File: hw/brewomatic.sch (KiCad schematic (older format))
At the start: 21 parts, among them J1 CON_MAX31865, J2 EXP1, J3 EXP2, J4 12V_IN, J5 12V_ALIM_CONN, J6 HEATING_CONN, J7 PUMP_CONN, Q1 BT139-600, Q2 IRF540N, U1 MOC3021M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

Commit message: Start layout of pcb
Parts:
- added J8: 12V_ALIM_CONN, Connectors_Terminal_Blocks:TerminalBlock_Pheonix_MKDS1.5-2pol, symbol Screw_Terminal_01x02
- J4, J6, J7: footprint Connectors_Terminal_Blocks:TerminalBlock_Pheonix_MPT-2.54mm_2pol -> Connectors_Terminal_Blocks:TerminalBlock_Pheonix_MKDS1.5-2pol
- J5: value 12V_ALIM_CONN -> 230V_CONN; footprint Connectors_Terminal_Blocks:TerminalBlock_Pheonix_MPT-2.54mm_2pol -> Connectors_Terminal_Blocks:TerminalBlock_Pheonix_MKDS1.5-2pol
- Q1: footprint TO_SOT_Packages_THT:TO-220_Neutral123_Vertical -> TO_SOT_Packages_THT:TO-220_Vertical
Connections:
- wire segments 94 -> 96
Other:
- moved on the sheet: J5
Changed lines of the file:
@@
 F 0 "Q1" H 5700 4475 50  0000 L CNN
 F 1 "BT139-600" H 5700 4400 50  0000 L CNN
-F 2 "TO_SOT_Packages_THT:TO-220_Neutral123_Vertical" H 5700 4325 50  0001 L CIN
+F 2 "TO_SOT_Packages_THT:TO-220_Vertical" H 5700 4325 50  0001 L CIN
 F 3 "" H 5500 4400 50  0000 L CNN
 	1    5500 4400
@@
 Wire Wire Line
 	8550 4650 8350 4650
-$Comp
-L +5V #PWR011
-U 1 1 5AB89F21
-P 7550 1650
-F 0 "#PWR011" H 7550 1500 50  0001 C CNN
-F 1 "+5V" H 7550 1790 50  0000 C CNN
-F 2 "" H 7550 1650 50  0001 C CNN
-F 3 "" H 7550 1650 50  0001 C CNN
-	1    7550 1650
-	1    0    0    -1
-$EndComp
 Wire Wire Line
 	7150 1650 7550 1650
@@
 F 0 "J4" H 4300 1200 50  0000 C CNN
 F 1 "12V_IN" H 4300 900 50  0000 C CNN
-F 2 "Connectors_Terminal_Blocks:TerminalBlock_Pheonix_MPT-2.54mm_2pol" H 4300 1100 50  0001 C CNN
+F 2 "Connectors_Terminal_Blocks:TerminalBlock_Pheonix_MKDS1.5-2pol" H 4300 1100 50  0001 C CNN
 F 3 "" H 4300 1100 50  0001 C CNN
 	1    4300 1100
@@
 $EndComp
 $Comp
-L GND #PWR012
+L GND #PWR011
 U 1 1 5AB9867E
 P 3700 1200
-F 0 "#PWR012" H 3700 950 50  0001 C CNN
+F 0 "#PWR011" H 3700 950 50  0001 C CNN
 F 1 "GND" H 3700 1050 50  0000 C CNN
 F 2 "" H 3700 1200 50  0001 C CNN
@@
 	3700 1200 4100 1200
 $Comp
-L +5V #PWR013
+L +5V #PWR012
 U 1 1 5AB987A9
 P 9250 2900
-F 0 "#PWR013" H 9250 2750 50  0001 C CNN
+F 0 "#PWR012" H 9250 2750 50  0001 C CNN
 F 1 "+5V" H 9250 3040 50  0000 C CNN
 F 2 "" H 9250 2900 50  0001 C CNN
@@
 	9250 2950 9250 2900
 $Comp
-L +12V #PWR014
+L +12V #PWR013
 U 1 1 5AB98837
 P 3700 1100
-F 0 "#PWR014" H 3700 950 50  0001 C CNN
+F 0 "#PWR013" H 3700 950 50  0001 C CNN
 F 1 "+12V" H 3700 1240 50  0000 C CNN
 F 2 "" H 3700 1100 50  0001 C CNN
@@
 	8550 3850 8150 3850
 $Comp
-L +3.3V #PWR015
+L +3.3V #PWR014
 U 1 1 5AB9D6E8
 P 9150 2750
-F 0 "#PWR015" H 9150 2600 50  0001 C CNN
+F 0 "#PWR014" H 9150 2600 50  0001 C CNN
 F 1 "+3.3V" H 9150 2890 50  0000 C CNN
 F 2 "" H 9150 2750 50  0001 C CNN
@@
 	9150 2950 9150 2750
 $Comp
-L +12V #PWR016
+L +12V #PWR015
 U 1 1 5AB9D78B
 P 8950 2800
-F 0 "#PWR016" H 8950 2650 50  0001 C CNN
+F 0 "#PWR015" H 8950 2650 50  0001 C CNN
 F 1 "+12V" H 8950 2940 50  0000 C CNN
 F 2 "" H 8950 2800 50  0001 C CNN
@@
 	8950 2950 8950 2800
 $Comp
-L GND #PWR017
+L GND #PWR016
 U 1 1 5AB9DCD3
 P 9050 5150
-F 0 "#PWR017" H 9050 4900 50  0001 C CNN
+F 0 "#PWR016" H 9050 4900 50  0001 C CNN
 F 1 "GND" H 9050 5000 50  0000 C CNN
 F 2 "" H 9050 5150 50  0001 C CNN
@@
 F 0 "J6" H 6550 5000 50  0000 C CNN
 F 1 "HEATING_CONN" H 6550 4700 50  0000 C CNN
-F 2 "Connectors_Terminal_Blocks:TerminalBlock_Pheonix_MPT-2.54mm_2pol" H 6550 4900 50  0001 C CNN
+F 2 "Connectors_Terminal_Blocks:TerminalBlock_Pheonix_MKDS1.5-2pol" H 6550 4900 50  0001 C CNN
 F 3 "" H 6550 4900 50  0001 C CNN
 	1    6550 4900
@@
 $EndComp
 $Comp
-L LINE #PWR018
+L LINE #PWR017
 U 1 1 5ABA2F2E
 P 5500 3850
-F 0 "#PWR018" H 5500 3700 50  0001 C CNN
+F 0 "#PWR017" H 5500 3700 50  0001 C CNN
 F 1 "LINE" H 5500 4000 50  0000 C CNN
 F 2 "" H 5500 3850 50  0001 C CNN
@@
 L Screw_Terminal_01x02 J5
 U 1 1 5ABA346E
-P 3000 1100
-F 0 "J5" H 3000 1200 50  0000 C CNN
-F 1 "12V_ALIM_CONN" H 3000 900 50  0000 C CNN
-F 2 "Connectors_Terminal_Blocks:TerminalBlock_Pheonix_MPT-2.54mm_2pol" H 3000 1100 50  0001 C CNN
-F 3 "" H 3000 1100 50  0001 C CNN
-	1    3000 1100
-	1    0    0    -1
-$EndComp
-$Comp
-L LINE #PWR019
+P 1750 1100
+F 0 "J5" H 1750 1200 50  0000 C CNN
+F 1 "230V_CONN" H 1750 900 50  0000 C CNN
+F 2 "Connectors_Terminal_Blocks:TerminalBlock_Pheonix_MKDS1.5-2pol" H 1750 1100 50  0001 C CNN
+F 3 "" H 1750 1100 50  0001 C CNN
+	1    1750 1100
+	1    0    0    -1
+$EndComp
+$Comp
+L LINE #PWR018
 U 1 1 5ABA3758
-P 2400 1200
-F 0 "#PWR019" H 2400 1050 50  0001 C CNN
-F 1 "LINE" H 2400 1350 50  0000 C CNN
-F 2 "" H 2400 1200 50  0001 C CNN
-F 3 "" H 2400 1200 50  0001 C CNN
-	1    2400 1200
+P 1150 1200
+F 0 "#PWR018" H 1150 1050 50  0001 C CNN
+F 1 "LINE" H 1150 1350 50  0000 C CNN
+F 2 "" H 1150 1200 50  0001 C CNN
+F 3 "" H 1150 1200 50  0001 C CNN
+	1    1150 1200
 	1    0    0    1
 $EndComp
 $Comp
+L NEUT #PWR019
+U 1 1 5ABA379C
+P 1150 1100
+F 0 "#PWR019" H 1150 950 50  0001 C CNN
+F 1 "NEUT" H 1150 1250 50  0000 C CNN
+F 2 "" H 1150 1100 50  0001 C CNN
+F 3 "" H 1150 1100 50  0001 C CNN
+	1    1150 1100
+	1    0    0    -1
+$EndComp
+Wire Wire Line
+	1150 1100 1550 1100
+Wire Wire Line
+	1150 1200 1550 1200
+$Comp
 L NEUT #PWR020
-U 1 1 5ABA379C
-P 2400 1100
-F 0 "#PWR020" H 2400 950 50  0001 C CNN
-F 1 "NEUT" H 2400 1250 50  0000 C CNN
-F 2 "" H 2400 1100 50  0001 C CNN
-F 3 "" H 2400 1100 50  0001 C CNN
-	1    2400 1100
-	1    0    0    -1
-$EndComp
-Wire Wire Line
-	2400 1100 2800 1100
-Wire Wire Line
-	2400 1200 2800 1200
-$Comp
-L NEUT #PWR021
 U 1 1 5ABA6182
 P 6100 4900
-F 0 "#PWR021" H 6100 4750 50  0001 C CNN
+F 0 "#PWR020" H 6100 4750 50  0001 C CNN
 F 1 "NEUT" H 6100 5050 50  0000 C CNN
 F 2 "" H 6100 4900 50  0001 C CNN
@@
 F 0 "J7" H 6550 6200 50  0000 C CNN
 F 1 "PUMP_CONN" H 6550 5900 50  0000 C CNN
-F 2 "Connectors_Terminal_Blocks:TerminalBlock_Pheonix_MPT-2.54mm_2pol" H 6550 6100 50  0001 C CNN
+F 2 "Connectors_Terminal_Blocks:TerminalBlock_Pheonix_MKDS1.5-2pol" H 6550 6100 50  0001 C CNN
 F 3 "" H 6550 6100 50  0001 C CNN
 	1    6550 6100
@@
 $EndComp
 $Comp
-L GND #PWR022
+L GND #PWR021
 U 1 1 5ABAE164
 P 6150 7000
-F 0 "#PWR022" H 6150 6750 50  0001 C CNN
+F 0 "#PWR021" H 6150 6750 50  0001 C CNN
 F 1 "GND" H 6150 6850 50  0000 C CNN
 F 2 "" H 6150 7000 50  0001 C CNN
@@
 	8550 4150 7900 4150
 $Comp
-L +12V #PWR023
+L +12V #PWR022
 U 1 1 5ABAF0C1
 P 6150 5800
-F 0 "#PWR023" H 6150 5650 50  0001 C CNN
+F 0 "#PWR022" H 6150 5650 50  0001 C CNN
 F 1 "+12V" H 6150 5940 50  0000 C CNN
 F 2 "" H 6150 5800 50  0001 C CNN
@@
 Wire Wire Line
 	5850 6650 5350 6650
+$Comp
+L +3.3V #PWR023
+U 1 1 5AB81819
+P 7550 1650
+F 0 "#PWR023" H 7550 1500 50  0001 C CNN
+F 1 "+3.3V" H 7550 1790 50  0000 C CNN
+F 2 "" H 7550 1650 50  0001 C CNN
+F 3 "" H 7550 1650 50  0001 C CNN
+	1    7550 1650
+	1    0    0    -1
+$EndComp
+$Comp
+L Screw_Terminal_01x02 J8
+U 1 1 5AB82AE1
+P 3000 1100
+F 0 "J8" H 3000 1200 50  0000 C CNN
+F 1 "12V_ALIM_CONN" H 3000 900 50  0000 C CNN
+F 2 "Connectors_Terminal_Blocks:TerminalBlock_Pheonix_MKDS1.5-2pol" H 3000 1100 50  0001 C CNN
+F 3 "" H 3000 1100 50  0001 C CNN
+	1    3000 1100
+	1    0    0    -1
+$EndComp
+$Comp
+L LINE #PWR024
+U 1 1 5AB82AE7
+P 2400 1200
+F 0 "#PWR024" H 2400 1050 50  0001 C CNN
+F 1 "LINE" H 2400 1350 50  0000 C CNN
+F 2 "" H 2400 1200 50  0001 C CNN
+F 3 "" H 2400 1200 50  0001 C CNN
+	1    2400 1200
+	1    0    0    1
+$EndComp
+$Comp
+L NEUT #PWR025
+U 1 1 5AB82AED
+P 2400 1100
+F 0 "#PWR025" H 2400 950 50  0001 C CNN
+F 1 "NEUT" H 2400 1250 50  0000 C CNN
+F 2 "" H 2400 1100 50  0001 C CNN
+F 3 "" H 2400 1100 50  0001 C CNN
+	1    2400 1100
+	1    0    0    -1
+$EndComp
+Wire Wire Line
+	2400 1100 2800 1100
+Wire Wire Line
+	2400 1200 2800 1200
 $EndSCHEMATC

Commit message: PCB routing done
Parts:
- added D5: LED_PUMP, LEDs:LED_1206_HandSoldering, symbol LED
- added D6: LED_TRIAC, LEDs:LED_1206_HandSoldering, symbol LED
- added R6, R7: 1K, Resistors_SMD:R_0805_HandSoldering, symbol R
- J4, J6, J7, J8: footprint Connectors_Terminal_Blocks:TerminalBlock_Pheonix_MKDS1.5-2pol -> TerminalBlock:TerminalBlock_bornier-2_P5.08mm
- J5: footprint Connectors_Terminal_Blocks:TerminalBlock_Pheonix_MKDS1.5-2pol -> TerminalBlock:TerminalBlock_bornier-3_P5.08mm; symbol Screw_Terminal_01x02 -> Screw_Terminal_01x03
- Q2: symbol IRF540N -> IRF540N-RESCUE-brewomatic
- R3: value R -> 220; footprint Resistors_THT:R_Axial_DIN0207_L6.3mm_D2.5mm_P10.16mm_Horizontal -> Resistors_SMD:R_0805_HandSoldering
- R4: value R -> 1K
- R5: value R -> 330
- U1: symbol MOC3021M -> MOC3021M-RESCUE-brewomatic
- U2: symbol 4N25 -> 4N25-RESCUE-brewomatic
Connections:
- net labels added: Earth, HEATING_LINE
- wire segments 96 -> 105
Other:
- moved on the sheet: R3, R5

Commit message: Less dangerous schematic !
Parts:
- removed D5: LED_PUMP, LEDs:LED_1206_HandSoldering, symbol LED
- removed D6: LED_TRIAC, LEDs:LED_1206_HandSoldering, symbol LED
- added C1: C, Capacitors_THT:C_Disc_D8.0mm_W5.0mm_P5.00mm, symbol C
- added D5: D, Diodes_THT:D_T-1_P10.16mm_Horizontal, symbol D
- added R8: 10K, Resistors_SMD:R_0805_HandSoldering, symbol R
- added R9: R, Resistors_THT:R_Axial_DIN0207_L6.3mm_D2.5mm_P10.16mm_Horizontal, symbol R
- added U3: 4N25, Housings_DIP:DIP-6_W7.62mm_Socket, symbol 4N25-RESCUE-brewomatic
- J5: footprint TerminalBlock:TerminalBlock_bornier-3_P5.08mm -> TerminalBlock:TerminalBlock_bornier-2_P5.08mm; symbol Screw_Terminal_01x03 -> Screw_Terminal_01x02
- Q1: footprint TO_SOT_Packages_THT:TO-220_Vertical -> HV_TO220:TO-220_Vertical_HV
- R6: value 1K -> 470
- R7: value 1K -> 100
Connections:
- net labels removed: Earth
- wire segments 105 -> 114
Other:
- moved on the sheet: J1, J7, Q2

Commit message: PCB: finalize layout
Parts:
- removed C1: C, Capacitors_THT:C_Disc_D8.0mm_W5.0mm_P5.00mm, symbol C
- removed R9: R, Resistors_THT:R_Axial_DIN0207_L6.3mm_D2.5mm_P10.16mm_Horizontal, symbol R
- R1: value R -> 45K
- R2: value R -> R45K
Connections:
- net HEATING_LINE: now also J6.1 (Pin_1); no longer J6.2 (Pin_2)
- net NEUT: now also J6.2 (Pin_2); no longer J6.1 (Pin_1)
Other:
- moved on the sheet: J6

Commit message: PCB: fix missing TEMP_CS pin and delete sd_detect
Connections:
- net TEMP_CS: now also A1.11 (D8)
- net TRIAC_CTRL: now also A1.10 (D7); no longer A1.11 (D8)
- net SD_DETECT: no longer names the net of J3.7
- net SD_DETECT: no longer A1.10 (D7)
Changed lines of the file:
@@
 Text Label 5900 1050 2    60   ~ 0
 ENC_E2
-Text Label 5900 1450 2    60   ~ 0
-SD_DETECT
 Text Label 7900 4550 2    60   ~ 0
 SPI_MISO
@@
 	1    0    0    -1
 $EndComp
-Text Label 7900 4150 2    60   ~ 0
-TRIAC_CTRL
 $Comp
 L +3.3V #PWR014
@@
 	-1   0    0    1
 $EndComp
-Text Label 8400 4050 2    60   ~ 0
-SD_DETECT
+Text Label 7900 4150 2    60   ~ 0
+TEMP_CS
 $Comp
 L IRF540N-RESCUE-brewomatic Q2
@@
 	6050 1250 5900 1250
 Wire Wire Line
-	5900 1450 6050 1450
-Wire Wire Line
 	6050 1650 5900 1650
 Wire Wire Line
@@
 Wire Wire Line
 	6200 5100 6350 5100
+Text Label 8400 4050 2    60   ~ 0
+TRIAC_CTRL
 $EndSCHEMATC

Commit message: HW: fix schematic for zero crossing input
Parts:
- removed R2: R45K, Resistors_THT:R_Axial_DIN0207_L6.3mm_D2.5mm_P10.16mm_Horizontal, symbol R
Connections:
- net at U2.2: now also D3.2 (A), D4.2 (A)
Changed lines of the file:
@@
-$EndComp
-$Comp
-L R R2
-U 1 1 5A7E1B17
-P 3550 2800
-F 0 "R2" V 3630 2800 50  0000 C CNN
-F 1 "R45K" V 3550 2800 50  0000 C CNN
-F 2 "Resistors_THT:R_Axial_DIN0207_L6.3mm_D2.5mm_P10.16mm_Horizontal" V 3480 2800 50  0001 C CNN
-F 3 "" H 3550 2800 50  0001 C CNN
-	1    3550 2800
-	0    1    1    0
 $EndComp
 $Comp
@@
 	3350 2600 3400 2600
 Wire Wire Line
-	3350 2800 3400 2800
-Wire Wire Line
 	3700 2600 4100 2600
 Connection ~ 4100 2600
-Wire Wire Line
-	3750 2800 3700 2800
 Wire Wire Line
 	2600 2900 2600 2800
@@
 Text Label 8400 4050 2    60   ~ 0
 TRIAC_CTRL
+Wire Wire Line
+	3750 2800 3350 2800
 $EndSCHEMATC

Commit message: PCB: update and fix LCD7/LCD5 swap
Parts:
- added D7, D8: LED, LEDs:LED_D5.0mm, symbol LED
- added J10: TEST_MOC, Pin_Headers:Pin_Header_Straight_1x02_Pitch2.54mm, symbol Conn_01x02
- added J9: TEST_IN, Pin_Headers:Pin_Header_Straight_1x02_Pitch2.54mm, symbol Conn_01x02
- added R10, R9: 220, Resistors_SMD:R_0805_HandSoldering, symbol R
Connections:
- net GND: now also D7.1 (K), D8.1 (K)
- net LCD5: now also A1.24 (A5), J2.6; no longer A1.12 (D9), J2.8
- net LCD7: now also A1.12 (D9), J2.8; no longer A1.24 (A5), J2.6
- net PUMP_CTRL: now also R10.2
- net TRIAC_CTRL: now also R9.2
- new net: D7.2 (A), R9.1
- new net: D8.2 (A), R10.1
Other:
- moved on the sheet: D1, D2, D3, D4, D5, J1, J4, J5, J6, J7, J8, Q1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

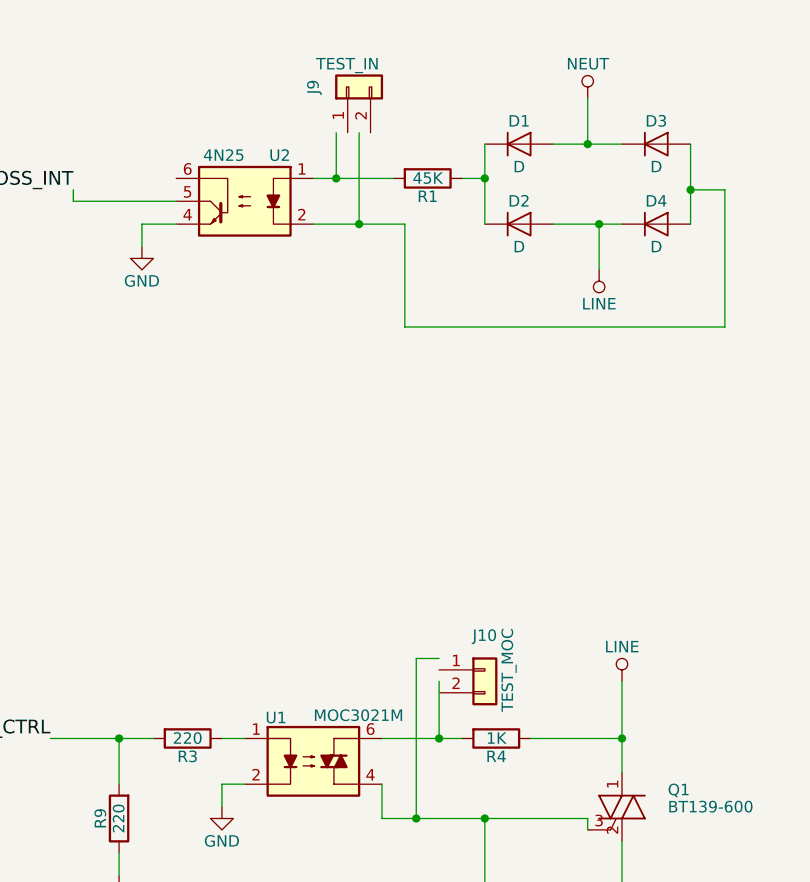
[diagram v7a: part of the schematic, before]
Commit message: Fix wrong pcb connection pcb
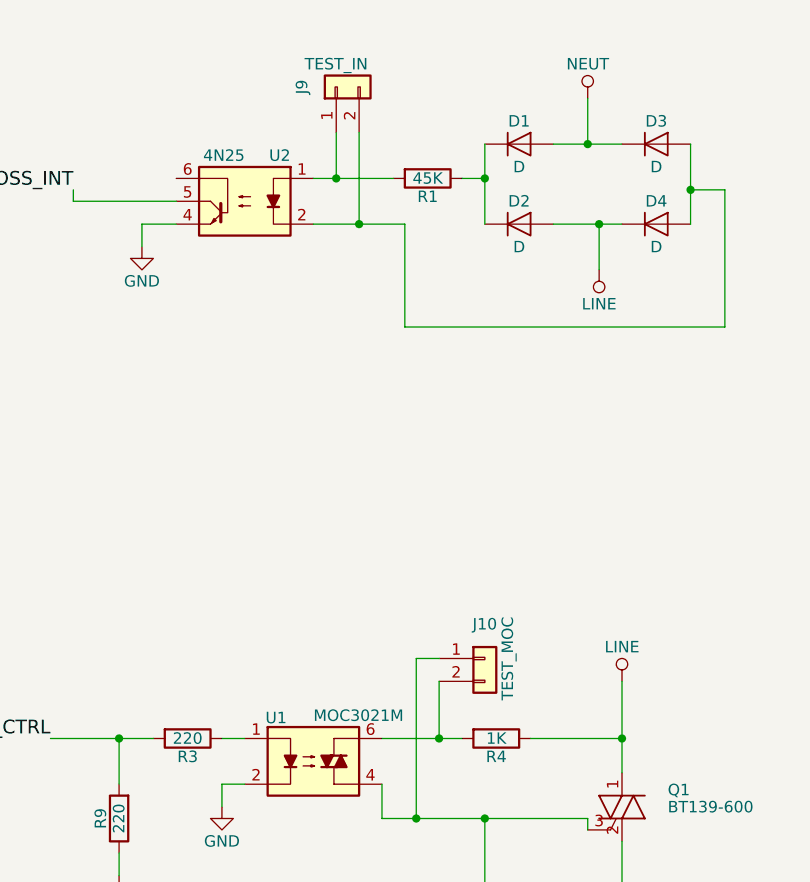
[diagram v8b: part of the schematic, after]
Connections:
- net at R1.2, U2.1: now also J9.1 (Pin_1)
- net at D3.2 (A), D4.2 (A), U2.2: now also J9.2 (Pin_2)
- net at Q1.3 (G), R5.2, U1.4: now also J10.1 (Pin_1)
- net at R4.2, U1.6: now also J10.2 (Pin_2)
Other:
- moved on the sheet: J10, J9
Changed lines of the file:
@@
 L Conn_01x02 J9
 U 1 1 5AC4B423
-P 2850 900
-F 0 "J9" H 2850 1050 50  0000 C CNN
-F 1 "TEST_IN" V 2950 900 50  0000 C CNN
-F 2 "Pin_Headers:Pin_Header_Straight_1x02_Pitch2.54mm" H 2850 900 50  0001 C CNN
-F 3 "" H 2850 900 50  0001 C CNN
-	1    2850 900
+P 2800 900
+F 0 "J9" H 2800 1050 50  0000 C CNN
+F 1 "TEST_IN" V 2900 900 50  0000 C CNN
+F 2 "Pin_Headers:Pin_Header_Straight_1x02_Pitch2.54mm" H 2800 900 50  0001 C CNN
+F 3 "" H 2800 900 50  0001 C CNN
+	1    2800 900
 	0    -1   -1   0
 $EndComp
@@
 L Conn_01x02 J10
 U 1 1 5AC4BD47
-P 3450 3450
-F 0 "J10" H 3450 3600 50  0000 C CNN
-F 1 "TEST_MOC" V 3550 3450 50  0000 C CNN
-F 2 "Pin_Headers:Pin_Header_Straight_1x02_Pitch2.54mm" H 3450 3450 50  0001 C CNN
-F 3 "" H 3450 3450 50  0001 C CNN
-	1    3450 3450
+P 3450 3400
+F 0 "J10" H 3450 3550 50  0000 C CNN
+F 1 "TEST_MOC" V 3550 3400 50  0000 C CNN
+F 2 "Pin_Headers:Pin_Header_Straight_1x02_Pitch2.54mm" H 3450 3400 50  0001 C CNN
+F 3 "" H 3450 3400 50  0001 C CNN
+	1    3450 3400
 	1    0    0    -1
 $EndComp
